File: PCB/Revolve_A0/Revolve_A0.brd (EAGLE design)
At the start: 123.9 x 100.1 mm, 442 parts, among them IC1 TMC2100-LA, IC10 74AHC1G126DCK, IC11 74AHC1G126DCK, IC12 TMC2100-LA, IC13 74AHC1G126DCK, IC14 74AHC1G126DCK, IC15 TMC2100-LA, IC16 74AHC1G126DCK, IC17 74AHC1G126DCK, IC18 74AHC1G126DCK, IC19 74AHC1G126DCK, IC2 TMC2100-LA, IC20 74AHC1G126DCK, IC21 74AHC1G126DCK, IC22 74AHC1G126DCK, IC24 TMC2100-LA, IC25 74AHC1G126DCK, IC26 74AHC1G126DCK, IC27 74AHC1G126DCK, IC28 74AHC1G126DCK, IC29 LAN8710A, IC3 74AHC1G126DCK, IC30 MTFC2GMDEA, IC31 CY7C65632, IC4 74AHC1G126DCK, IC5 TMC2100-LA, IC6 74AHC1G126DCK, IC7 74AHC1G126DCK, IC8 74AHC1G126DCK, IC9 74AHC1G126DCK, J1 USD_CONNECTOR, Q1 AON6758, Q2 AON6758, Q3 AON6758, Q8 AON6758, U1 SN74AHC595PW, U10 TPD4S012_DRY_6, U11 PCA9685PW, U18 CAT24C256, U19 CD4050BD, U2 SN74AHC595PW, U3 SN74AHC595PW, U4 SN74AHC595PW, U5 SN74AHC595PW, U6 RT8268, U8 SN74AHC595PW, X1 22-05-7038-03, X10 22-05-7038-03, X11 22-05-7038-03, X12 22-05-7048-04, X13 22-05-7038-03, X14 22-05-7048-04, X15 22-05-7048-04, X16 22-05-7048-04, X17 22-05-7048-04, X18 22-05-7048-04, X19 22-05-7038-03, X2 MSTBA4, X20 MSTBA4, X21 MSTBA2, X22 22-05-7038-03, X23 22-05-7038-03, X24 HDMI, X25 22-05-7048-04, X26 MSTBA2, X27 MINI-USB_SHIELD5P4-32005-400, X29 22-05-7038-03, X3 MSTBA2, X4 22-05-7028-02, X5 22-05-7028-02, X6 22-05-7028-02, X7 22-05-7038-03, X8 22-05-7038-03, X9 22-05-7028-02, Y1 24MHz, Y2 32.768 MHz, Y3 25 MHz, Y4 12 MHz

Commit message: Starting up work again
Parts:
- removed C14, C15, C24, C41, C42, C5, C84, C85, C86, C87, C88, C99: 0.1uF, rcl:C0402
- removed IC10, IC11, IC13, IC14, IC16, IC17, IC18, IC19, IC20, IC21, IC22, IC25, IC26, IC27, IC3, IC4, IC8, IC9: 74AHC1G126DCK, 74xx-little-de:SC70-5
- removed U1, U2, U3, U4, U5, U8: SN74AHC595PW, sn74hc595:SOP65P640X120-16N
- moved R151 61.5 mm to (102.5, 70.1)
- moved C155 55.6 mm to (102.8, 68.1)
- moved C154 13.7 mm to (119.0, 28.6), turned to 90 degrees
- moved C153 12.4 mm to (120.2, 28.6), turned to 90 degrees
- moved R88 4.49 mm to (105.7, 72.5)
- moved IC31 4.43 mm to (102.3, 70.5)
- moved R92 2.54 mm to (99.5, 85.0)
- moved R94 1.04 mm to (99.1, 88.8)
- moved C112 0.43 mm to (98.6, 77.5)
- moved C114 0.39 mm to (96.3, 77.5)
- moved C108 0.32 mm to (85.6, 84.7)
- moved C115 0.32 mm to (85.6, 85.8)
- moved U$7 0.32 mm to (92.8, 83.8)
- moved R93 0.12 mm to (99.1, 87.8)
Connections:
- removed net EN_EHA: IC19.2, IC22.2, IC27.2, U4.15
- removed net EN_XYZ: IC18.2, IC20.2, IC21.2, U1.15
- removed net N$103: IC17.1, U5.7
- removed net N$104: IC17.2, U5.6
- removed net N$105: IC16.1, U5.5
- removed net N$106: IC16.2, U5.4
- removed net N$142: IC26.1, U8.7
- removed net N$143: IC26.2, U8.6
- removed net N$144: IC25.2, U8.4
- removed net N$146: IC25.1, U8.5
- removed net N$34: IC3.2, U1.4
- removed net N$4: IC4.1, U1.7
- removed net N$40: IC3.1, U1.5
- removed net N$5: IC4.2, U1.6
- removed net N$59: IC11.1, U3.7
- removed net N$61: IC11.2, U3.6
- removed net N$62: IC10.1, U3.5
- removed net N$63: IC10.2, U3.4
- removed net N$66: IC9.1, U2.7
- removed net N$67: IC9.2, U2.6
- removed net N$68: IC8.1, U2.5
- removed net N$69: IC8.2, U2.4
- removed net N$85: IC14.1, U4.7
- removed net N$86: IC14.2, U4.6
- removed net N$87: IC13.1, U4.5
- removed net N$93: IC13.2, U4.4
- removed net SER6: U5.9
- removed net SER_2: U1.9, U2.14
- removed net SER_3: U2.9, U3.14
- removed net SER_4: U3.9, U4.14
- removed net SER_5: U4.9, U5.14
- removed net SER_6: U8.14
- removed net TRISTATE_STEPPERS: IC18.1, IC19.1, IC20.1, IC21.1, IC22.1, IC27.1, U5.15, U8.15
- net +3V3: no longer C14.1, C15.1, C24.1, C41.1, C42.1, C5.1, C84.1, C85.1, C86.1, C87.1, C88.1, C99.1, IC10.5, IC11.5, IC13.5, IC14.5, IC16.5, IC17.5, IC18.5, IC19.5, IC20.5, IC21.5, IC22.5, IC25.5, IC26.5, IC27.5, IC3.5, IC4.5, IC8.5, IC9.5, U1.10, U1.16, U2.10, U2.16, U3.10, U3.16, U4.10, U4.16, U5.10, U5.16, U8.10, U8.16
- net ENABLE_A: no longer IC27.4
- net ENABLE_E: no longer IC19.4
- net ENABLE_H: no longer IC22.4
- net ENABLE_X: no longer IC18.4
- net ENABLE_Y: no longer IC20.4
- net ENABLE_Z: no longer IC21.4
- net GND: no longer C14.2, C15.2, C24.2, C41.2, C42.2, C5.2, C84.2, C85.2, C86.2, C87.2, C88.2, C99.2, IC10.3, IC11.3, IC13.3, IC14.3, IC16.3, IC17.3, IC18.3, IC19.3, IC20.3, IC21.3, IC22.3, IC25.3, IC26.3, IC27.3, IC3.3, IC4.3, IC8.3, IC9.3, U1.13, U1.8, U2.13, U2.8, U3.13, U3.8, U4.13, U4.8, U5.13, U5.8, U8.13, U8.8
- net N$100: no longer U5.3
- net N$101: no longer U5.2
- net N$102: no longer U5.1
- net N$133: no longer IC25.4
- net N$138: no longer IC26.4
- net N$139: no longer U8.3
- net N$140: no longer U8.2
- net N$141: no longer U8.1
- net N$28: no longer IC10.4
- net N$42: no longer IC8.4
- net N$43: no longer U1.1
- net N$44: no longer U1.3
- net N$49: no longer IC9.4
- net N$53: no longer U2.3
- net N$54: no longer IC11.4
- net N$55: no longer U3.3
- net N$56: no longer U2.2
- net N$57: no longer U3.2
- net N$58: no longer U3.1
- net N$6: no longer U1.2
- net N$65: no longer U2.1
- net N$76: no longer IC13.4
- net N$81: no longer IC14.4
- net N$82: no longer U4.3
- net N$83: no longer U4.2
- net N$84: no longer U4.1
- net N$91: no longer IC16.4
- net N$99: no longer IC17.4
- net SERVO_0_EN: no longer U2.15
- net SERVO_1_EN: no longer U3.15
- net SPI1_CS1: no longer U1.12, U2.12, U3.12, U4.12, U5.12, U8.12
- net SPI1_MOSI: no longer U1.14
- net SPI1_SCLK: no longer U1.11, U2.11, U3.11, U4.11, U5.11, U8.11
- net X_CFG1: no longer IC4.4
- net X_CFG2: no longer IC3.4
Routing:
- net SYS_5V: track 20.0 -> 99.4 mm, vias 0 -> 4
- net SPI1_CS1: track 76.3 -> 8.89 mm, vias 5 -> 0
- net TRISTATE_STEPPERS: track 61.5 -> 0.00 mm, vias 6 -> 0
- net 12MHZ: track 0.00 -> 45.1 mm, vias 0 -> 2
- net EN_XYZ: track 39.5 -> 0.00 mm, vias 4 -> 0
- net N$186: track 0.00 -> 27.7 mm, vias 0 -> 2
- net EN_EHA: track 26.1 -> 0.00 mm, vias 3 -> 0
- net N$185: track 0.00 -> 23.2 mm, vias 0 -> 2
- net N$1: track 0.00 -> 20.4 mm, vias 0 -> 2
- net SPI1_SCLK: track 16.8 -> 0.00 mm, vias 2 -> 0
- net +3V3: track 237.3 -> 222.9 mm, vias 23 -> 20
- net SER_2: track 13.4 -> 0.00 mm, vias 2 -> 0
- net SER_5: track 12.9 -> 0.00 mm, vias 2 -> 0
- net SER_3: track 12.9 -> 0.00 mm, vias 2 -> 0
- net SER_4: track 12.1 -> 0.00 mm, vias 2 -> 0
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- added copper zone on layer 3, net HDMI_1V8

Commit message: Started porting to SIP-SM, changed to TMC2130
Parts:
- removed C13, C153: 0.1uF, rcl:C0402
- removed C154: 10uF, rcl:C0402
- removed IC28: 74AHC1G126DCK, 74xx-little-de:SC70-5
- removed J1: USD_CONNECTOR, BeagleBone_Blue:MICRO-SD-SOCKET-PP
- removed R142, R143, R144, R145, R146: 4.7K, rcl:R0402
- removed TP1, TP2, TP3, TP4: TPPAD1-13, testpad:P1-13
- removed U$10, U$8: IP4283CZ10-TBR, Revolve:UDFN
- removed U18: CAT24C256, custom:SOIC127P600X175-8N
- removed Y2: 32.768 MHz, Revolve:FX135A-327
- added C15, C24, C84, C85, C87, C99: 0.1uF, rcl:C0402
- added C41: 10uF, rcl:C0805
- added C42: 100uF, Panasonic-EEEFK_EEEFP:RHS1V10MCN1GS
- added C86: 4.7uF, rcl:C0402
- added C88: 22nF, rcl:C0402
- added EEPROM_WP, PMIC_NRESET, SYS_5V, SYS_RTC_1V8, SYS_VDD1_3V3, SYS_VDD2_3V3, SYS_VDD3_3V3, VDDS_DDR, VDDS_PLL, VDD_CODE, VDD_MPU: TPPAD1-13, testpad:P1-13
- added R153: 22R, rcl:R0402
- added SV2: (no value), con-lstb:MA05-1
- added U$11, U$12: DF10G7M1N, Revolve:DF10G7M1N
- added U1: OSD3358-512M-BSM, Octavo-Systems:OSD335X-BGA-256
- C144, C145: value 18pF -> 4.7uF
- C152: value 0.1uF -> 0.001uF
- R126: value 22R -> 2.2R
- R138: value 4.7K -> 0.1R; device rcl:R0402 -> rcl:R0805
- R139: value 1.5K -> 0.1R; device rcl:R0402 -> rcl:R0805
- R140: value 1.5K -> 10K
- R141: value 4.7K -> 10K
- R149: value 1M -> 0.1,5%
- U$2: value OSD3358-PARTS -> TRINAMIC_TMC2130_QFN36; device OSD3358-BAS-2:BGA400 -> TMC2130-Eval_v13:TRINAMIC_QFN36
- moved R141 307.0 mm to (-12.4, -250.9), turned to 0 degrees
- moved C145 297.9 mm to (-12.4, -241.4), turned to 0 degrees
- moved R126 297.4 mm to (-6.50, -210.3), turned to 0 degrees
- moved C144 295.5 mm to (-12.4, -236.6), turned to 0 degrees
- moved R140 291.9 mm to (-12.4, -246.1), turned to 0 degrees
- moved R138 283.1 mm to (-11.9, -225.2), turned to 0 degrees
- moved R139 276.9 mm to (-11.9, -231.2), turned to 0 degrees
- moved JP2 156.2 mm to (139.4, 89.3)
- moved R149 112.9 mm to (-12.4, -48.2), turned to 0 degrees
- moved C105 71.1 mm to (114.7, 10.1)
- moved LED10 71.1 mm to (121.8, 19.9)
- moved LED11 71.1 mm to (121.8, 18.8)
- moved LED12 71.1 mm to (121.8, 17.6)
- moved LED13 71.1 mm to (121.8, 8.22)
- moved LED9 71.1 mm to (121.8, 21.1)
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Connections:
- removed net GPIO1_16: U$2.R13
- removed net GPIO2_0: U$2.T13
- removed net GPIO3_21: U$2.V17
- removed net LCD_VCLK: R126.1, U$7.4
- removed net LDO_PGOOD: U$2.B20, U$2.B5
- removed net MMC0_CD: J1.CD1, R146.1, U$2.C15
- removed net MMC0_CLK: J1.CLK, R138.1, U$2.G17
- removed net MMC0_CMD: J1.CMD, R141.1, U$2.G18
- removed net MMC0_DAT0: J1.DAT0, R142.1, U$2.G16
- removed net MMC0_DAT1: J1.DAT1, R143.1, U$2.G15
- removed net MMC0_DAT2: J1.DAT2, R144.1, U$2.F18
- removed net MMC0_DAT3: J1.CD/DAT3, R145.1, U$2.F17
- removed net N$182: U$2.D13
- removed net N$211: U$2.R7
- removed net PMIC_INT: U$2.B19
- removed net PMIC_NWAKEUP: U$2.A19, U$2.C5
- removed net PMIC_PGOOD: IC28.2, U$2.A20, U$2.B15
- removed net PMIC_POWER_EN: U$2.C6, U$2.D19
- removed net SPI1_CS1: U$2.C18
- removed net SPI1_MISO: U$2.B13
- removed net SPI1_MOSI: U$2.D12
- removed net SPI1_SCLK: U$2.A13
- removed net VDD_1V8: L3.2, U$2.N16, U$2.R16
- removed net VDD_3V3A: U$2.E10, U$2.E11, U$2.E12, U$2.E13, U$2.F14, U$2.G14, U$2.H14, U$2.J14, U$2.K14, U$2.L14, U$2.N15, U$2.N5, U$2.P10, U$2.P11, U$2.P12, U$2.P13, U$2.P5, U$2.P6, U$2.P7, U$2.P8, U$2.R15
- removed net VDD_3V3AUX: R89.2, U$2.Y11
- removed net VDD_RTC: IC28.1, IC28.5, U$2.D7, U$2.E14, U$2.E6, U$2.F9, U$2.K13, U$2.N6, U$2.P14, U$2.P9
- new net CGND: R149.2
- new net DIR_B: U1.B15
- new net DIR_C: U1.R6
- new net IREF_X1: C145.1, R140.2, R141.1
- new net LCD_PCLK: R153.1, U$7.4, U1.F1
- new net N$103: U1.C10, U1.D10
- new net N$104: U1.C11, U1.D11
- new net N$105: SYS_VDD1_3V3.TP, U1.F6, U1.F7, U1.G6, U1.G7
- new net N$106: U$2.21
- new net N$120: SYS_VDD3_3V3.TP, U1.F8, U1.G8, U1.H7, U1.H8, U1.J7, U1.J8, U1.K8, U1.L8
- new net N$142: SYS_RTC_1V8.TP, U1.K11, U1.L11
- new net N$143: U1.L4, U1.M4
- new net N$144: U1.D4, U1.E4
- new net N$146: U1.F9, U1.G9, U1.H9, U1.J9, U1.K9, U1.L9
- new net N$161: U$2.20
- new net N$162: PMIC_NRESET.TP, U1.M13
- new net N$165: U1.T7
- new net N$166: C86.2, R126.1, U$2.25
- new net N$167: C87.1, R126.2, U$2.26
- new net N$168: C88.2, U$2.27
- new net N$170: C88.1, U$2.28
- new net N$171: C99.1, U$2.29
- new net N$188: U1.R12
- new net N$189: U1.P12
- new net N$190: U1.T13
- new net N$215: SV2.4, U1.A12
- new net N$34: U1.F4, VDDS_DDR.TP
- new net N$4: SV2.3, U1.C12
- new net N$40: U1.G4, VDD_CODE.TP
- new net N$5: SV2.2, U1.C13
- new net SPI0_CS0: U1.A14
- new net SPI0_CS1: U1.C14
- new net SPI0_CSX: U$2.2
- new net SPI0_MISO: U$2.5, U1.B13
- new net SPI0_MOSI: U$2.4, U1.B14
- new net SPI0_SCLK: U$2.3, U1.A13
- new net STEP_B: U1.B16
- new net STEP_C: U1.P6
- new net SYS_VDD2_3V3: R89.2, SYS_VDD2_3V3.TP, U1.F11, U1.G11
- new net SYS_VDD_1V8: L3.2, U1.F10, U1.G10, U1.H10, U1.H11, U1.J10, U1.J11, U1.K10, U1.L10
- new net VDDS_PLL: U1.G13, VDDS_PLL.TP
- new net VDD_MPU: U1.F13, VDD_MPU.TP
- new net VIN_BAT: U1.P8, U1.R8, U1.T8
- net +24V: now also C15.1, C24.1, C41.1, C42.+, C85.2, C99.2, U$2.16, U$2.30, U$2.31
- net +3V3: now also C84.1, U$2.8; no longer C13.1, C153.1, C154.1, J1.VCC, R138.2, R139.2, R140.2, R141.2, R142.2, R143.2, R144.2, R145.2, R146.2, U$2.U20, U$2.V20, U18.3, U18.8
- net +5V: now also U1.P10, U1.R10, U1.T10; no longer U$2.Y5, U$2.Y6
- net DIR_A: now also U1.A16
- net DIR_E: now also U1.C4; no longer U$2.U13
- net DIR_H: now also U1.C16; no longer U$2.V13
- net DIR_X: now also U$2.7, U1.A2; no longer U$2.V6
- net DIR_Y: now also U1.B1; no longer U$2.U10
- net DIR_Z: now also U1.B3; no longer U$2.T11
- net EMMC_RST: now also U1.R13; no longer U$2.R14
- net ENABLE: no longer U$2.D14
- net END_STOP_X_1: no longer U$2.A14
- net END_STOP_X_2: no longer U$2.T17
- net END_STOP_Y_1: no longer U$2.V14
- net END_STOP_Y_2: no longer U$2.C12
- net END_STOP_Z_1: no longer U$2.U17
- net END_STOP_Z_2: no longer U$2.B16
- net FAULT_E: no longer U$2.V12
- net FAULT_H: no longer U$2.T7
- net FAULT_X: no longer U$2.U6
- net FAULT_Y: no longer U$2.T6
- net FAULT_Z: no longer U$2.D15
- net GND: now also C144.2, C145.2, C15.2, C24.2, C41.2, C42.-, C84.2, C85.1, C86.1, C87.2, R138.1, R139.1, R149.1, SV2.1, U$11.3, U$12.3, U$2.11, U$2.12, U$2.24, U$2.35, U$2.36, U$2.GND_PAD, U1.D8, U1.D9, U1.E10, U1.E11, U1.E12, U1.E5, U1.E6, U1.E7, U1.E8, U1.E9, U1.F12, U1.F5, U1.G12, U1.G5, U1.H12, U1.H13, U1.H4, U1.H5, U1.J12, U1.J13, U1.J4, U1.J5, U1.K12, U1.K5, U1.L12, U1.L5, U1.M10, U1.M11, U1.M12, U1.M5, U1.M6, U1.M7, U1.M8, U1.M9, U1.N8, U1.N9; no longer C13.2, C153.2, C154.2, IC28.3, J1.GND, J1.GND1, J1.GND3, U$10.3, U$10.8, U$2.A1, U$2.A18, U$2.E19, U$2.E20, U$2.F19, U$2.F8, U$2.G11, U$2.G12, U$2.G19, U$2.G8, U$2.G9, U$2.H10, U$2.H12, U$2.H19, U$2.H6, U$2.H7, U$2.H8, U$2.H9, U$2.J10, U$2.J11, U$2.J19, U$2.J20, U$2.J6, U$2.J7, U$2.J8, U$2.J9, U$2.K10, U$2.K11, U$2.K19, U$2.K7, U$2.K9, U$2.L10, U$2.L11, U$2.L12, U$2.L13, U$2.L19, U$2.M10, U$2.M12, U$2.M14, U$2.M19, U$2.M6, U$2.M7, U$2.M8, U$2.M9, U$2.N10, U$2.N11, U$2.N14, U$2.N19, U$2.N20, U$2.N7, U$2.P19, U$2.P20, U$2.R19, U$2.R20, U$2.T19, U$2.T20, U$2.U19, U$2.V1, U$2.V18, U$2.V19, U$2.W10, U$2.W11, U$2.W12, U$2.W13, U$2.W14, U$2.W15, U$2.W16, U$2.W17, U$2.W18, U$2.W19, U$2.W2, U$2.W20, U$2.W3, U$2.W5, U$2.W6, U$2.W7, U$2.W8, U$2.W9, U$2.Y10, U$2.Y12, U$2.Y15, U$2.Y18, U$2.Y7, U$8.3, U$8.8, U18.1, U18.2, U18.4
- net GNDA_ADC: now also U1.A9; no longer U$2.A6, U$2.A9, U$2.E8
- net HDMI_INT: now also U1.T15; no longer U$2.U16
- net I2C0_SCL: no longer R140.1, U$2.C16, U$2.C20, U18.6
- net I2C0_SDA: no longer R139.1, U$2.C17, U$2.C19, U18.5
- net IREF_X_RAW: now also R141.2
- net LCD_D0: now also U1.G3; no longer U$2.R1
- net LCD_D1: now also U1.G2; no longer U$2.R2
- net LCD_D10: now also U1.K2; no longer U$2.U3
- net LCD_D11: now also U1.K1; no longer U$2.U4
- net LCD_D12: now also U1.L3; no longer U$2.V2
- net LCD_D13: now also U1.L2; no longer U$2.V3
- net LCD_D14: now also U1.L1; no longer U$2.V4
- net LCD_D15: now also U1.M3; no longer U$2.T5
- net LCD_D2: now also U1.G1; no longer U$2.R3
- net LCD_D3: now also U1.H3; no longer U$2.R4
- net LCD_D4: now also U1.H2; no longer U$2.T1
- net LCD_D5: now also U1.H1; no longer U$2.T2
- net LCD_D6: now also U1.J3; no longer U$2.T3
- net LCD_D7: now also U1.J2; no longer U$2.T4
- net LCD_D8: now also U1.J1; no longer U$2.U1
- net LCD_D9: now also U1.K3; no longer U$2.U2
- net LCD_DE: now also R153.2, U1.E1; no longer U$2.R6
- net LCD_HSYNC: now also U1.F2; no longer U$2.R5
- net LCD_VSYNC: now also U1.F3; no longer U$2.U5
- net MDIO_CLK: now also U1.D13; no longer U$2.M18
- net MDIO_DATA: now also U1.E13; no longer U$2.M17
- net MII1_COL: now also U1.F15; no longer U$2.H16
- net MII1_CRS_DV: now also U1.F14; no longer U$2.H17
- net MII1_RXCLK: now also U1.E16; no longer U$2.L18
- net MII1_RXD0: now also U1.E14; no longer U$2.M16
- net MII1_RXD1: now also U1.D16; no longer U$2.L15
- net MII1_RXD2: now also U1.D15; no longer U$2.L16
- net MII1_RXD3: now also U1.D14; no longer U$2.L17
- net MII1_RXDV: now also U1.F16; no longer U$2.J17
- net MII1_RXERR: now also U1.E15; no longer U$2.J15
- net MII1_TXCLK: now also U1.H16; no longer U$2.K18
- net MII1_TXD0: now also U1.H15; no longer U$2.K17
- net MII1_TXD1: now also U1.H14; no longer U$2.K16
- net MII1_TXD2: now also U1.G16; no longer U$2.K15
- net MII1_TXD3: now also U1.G15
- net MII1_TXEN: now also U1.G14; no longer U$2.J16, U$2.J18
- net MMC1_CLK: now also U1.P2; no longer U$2.U9
- net MMC1_CMD: now also U1.P1; no longer U$2.V9
- net MMC1_DAT0: now also U1.R3; no longer U$2.U7
- net MMC1_DAT1: now also U1.R2; no longer U$2.V7
- net MMC1_DAT2: now also U1.R1; no longer U$2.R8
- net MMC1_DAT3: now also U1.T3; no longer U$2.T8
- net MMC1_DAT4: now also U1.T2; no longer U$2.U8
- net MMC1_DAT5: now also U1.T1; no longer U$2.V8
- net MMC1_DAT6: now also U1.P4; no longer U$2.R9
- net MMC1_DAT7: now also U1.R4; no longer U$2.T9
- net N$1: now also U1.N10, U1.N11; no longer TP1.TP, U$2.E16
- net N$121: now also U1.N4, U1.N5; no longer TP2.TP, U$2.E15
- net N$172: now also R138.2, U$2.14; no longer C144.2, R149.1, U$2.H20, Y2.P$1
- net N$173: now also R139.2, U$2.33; no longer C145.2, R149.2, U$2.F20, Y2.P$2
- net N$174: now also EEPROM_WP.TP, U1.M2; no longer C144.1, C145.1, U$2.G20
- net N$175: no longer U$2.B10
- net N$176: now also U1.P16; no longer U$2.M20
- net N$177: now also U1.N15; no longer U$2.L20
- net N$178: now also U1.T16; no longer U$2.C13
- net N$179: now also U1.T11; no longer U$2.D20
- net N$184: now also U1.N16; no longer U$2.K20
- net N$185: now also C144.1, R140.1, U$2.23; no longer TP3.TP, U$2.E18
- net N$186: now also U1.T12; no longer TP4.TP, U$2.E17
- net N$210: now also SV2.5, U1.B12; no longer R126.2, U$2.V5
- net SERVO_0: no longer U$2.U14
- net SERVO_1: no longer U$2.T14
- net STEP_A: now also U1.A15
- net STEP_E: now also U1.C3; no longer U$2.U18
- net STEP_H: now also U1.C15; no longer U$2.R12
- net STEP_X: now also U$2.6, U1.A1; no longer U$2.U12
- net STEP_Y: now also U1.B2; no longer U$2.T12
- net STEP_Z: now also U1.A3; no longer U$2.T10
- net SYS_5V: now also SYS_5V.TP, U1.K6, U1.K7, U1.L6, U1.L7; no longer U$2.W4, U$2.Y4
- net SYS_RESETN: no longer IC28.4, U$2.A10
- net TERM_A: now also U1.C6; no longer U$2.A7
- net TERM_E: now also U1.A8; no longer U$2.B6
- net TERM_H: now also U1.B6; no longer U$2.B7
- net TERM_HBP: now also U1.B8; no longer U$2.C7
- net TX0+: now also U$12.5, U$12.6; no longer U$8.5
- net TX0-: now also U$12.4, U$12.7; no longer U$8.4
- net TX1+: now also U$11.2, U$11.9; no longer U$10.2
- net TX1-: now also U$11.1, U$11.10; no longer U$10.1
- net TX2+: now also U$11.5, U$11.6; no longer U$10.5
- net TX2-: now also U$11.4, U$11.7; no longer U$10.4
- net TXC+: now also U$12.2, U$12.9; no longer U$8.2
- net TXC-: now also U$12.1, U$12.10; no longer U$8.1
- net USB0_DM: now also U1.K16; no longer U$2.N18
- net USB0_DP: now also U1.K15; no longer U$2.N17
- net USB0_ID: now also U1.K14; no longer U$2.P16
- net USB1_DM: now also U1.L16; no longer U$2.R18
- net USB1_DP: now also U1.L15; no longer U$2.R17
- net USB1_OCN: now also U1.R15; no longer U$2.T16
- net USB_DC: now also U1.J16, U1.P9, U1.R9, U1.T9; no longer U$2.P15, U$2.Y8, U$2.Y9
- net USR0: now also U1.P13; no longer U$2.V15
- net USR1: now also U1.T14; no longer U$2.U15
- net USR2: now also U1.R14; no longer U$2.T15
- net USR3: now also U1.P14; no longer U$2.V16
- net VDD_ADC: now also U1.A7, U1.B7; no longer U$2.A4, U$2.A5, U$2.B9
- net XDMA_EVENT_INTR0: now also U1.A4; no longer U$2.A15
- net X_A1: now also U$2.34; no longer IC1.34
- net X_A2: now also U$2.32; no longer IC1.32
- net X_B1: now also U$2.13; no longer IC1.13
- net X_B2: now also U$2.15; no longer IC1.15
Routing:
- net MMC0_CLK: track 109.0 -> 0.00 mm, vias 4 -> 0
- net MMC0_DAT0: track 108.5 -> 0.00 mm, vias 4 -> 0
- net MMC0_DAT1: track 107.9 -> 0.00 mm, vias 4 -> 0
- net MMC0_DAT3: track 106.0 -> 0.00 mm, vias 4 -> 0
- net MMC0_CD: track 97.1 -> 0.00 mm, vias 2 -> 0
- net DIR_E: track 116.2 -> 26.0 mm, vias 7 -> 3
- net FAULT_E: track 109.7 -> 30.2 mm, vias 6 -> 3
- net USR3: track 78.4 -> 0.00 mm, vias 2 -> 0
- net MMC0_DAT2: track 77.5 -> 0.00 mm, vias 4 -> 0
- net USR0: track 77.2 -> 0.00 mm, vias 2 -> 0
- net USB1_DM: track 54.9 -> 0.00 mm, vias 1 -> 0
- net USB1_DP: track 53.8 -> 0.00 mm, vias 1 -> 0
- net MMC0_CMD: track 52.7 -> 0.00 mm, vias 3 -> 0
- net +3V3: track 222.9 -> 173.9 mm, vias 20 -> 18
- net LCD_VCLK: track 48.5 -> 0.00 mm, vias 4 -> 0
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
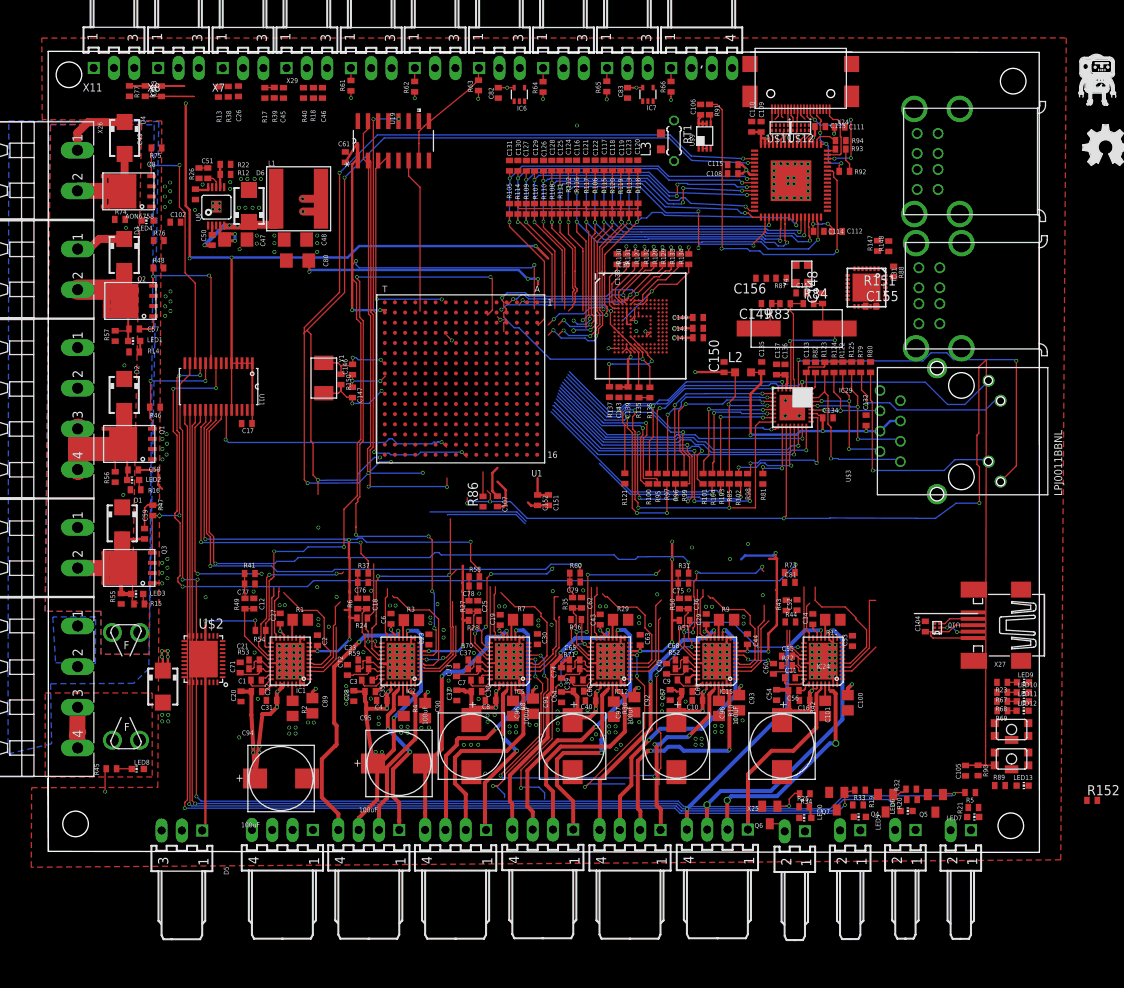
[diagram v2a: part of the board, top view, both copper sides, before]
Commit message: New Step down, moved some stuff around
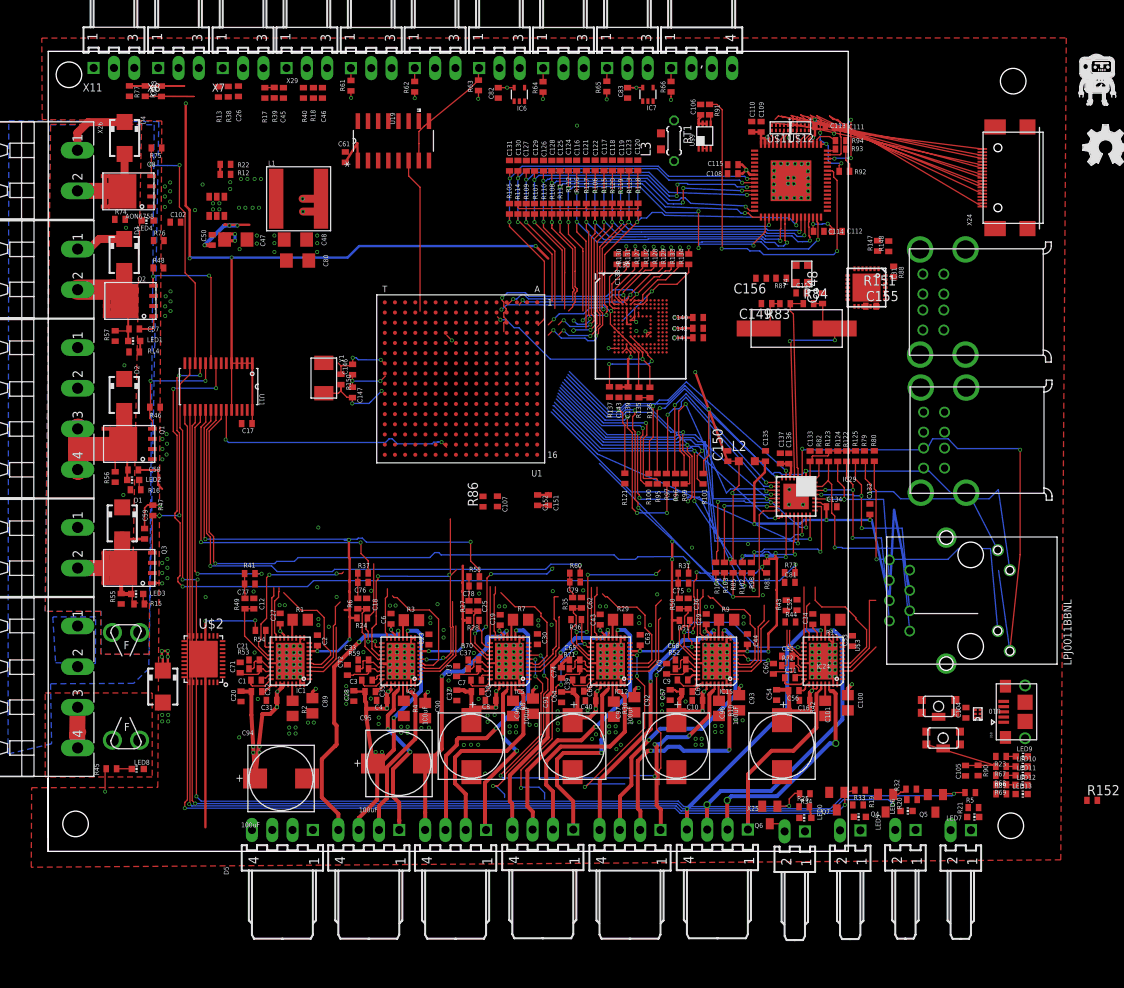
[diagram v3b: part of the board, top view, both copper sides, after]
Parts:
- removed C49: 10nF, rcl:C0402
- removed C51: 1nF, rcl:C0402
- removed D6: MBRA340T3, diode:SMA
- removed R26: 39K, rcl:R0402
- removed U6: RT8268, SparkFun:MSOP10
- removed X23: 22-05-7038-03, con-molex:7395-03
- removed X27: MINI-USB_SHIELD5P4-32005-400, con-cypressindustries:32005-400
- added U$10: TPS54202, Texas Instruments_By_element14_Batch_1:SOT23
- added U$8: USB-MICRO, Manga_screen_rev_B-3:USB-MICRO
- moved X24 26.3 mm to (118.4, 84.2), turned to 90 degrees
- moved U$3 21.2 mm to (115.3, 31.3)
- moved U$6 18.1 mm to (114.8, 51.4)
- moved U$5 17.6 mm to (114.7, 68.7)
- moved C104 11.9 mm to (114.7, 17.3)
- moved U10 11.9 mm to (116.2, 17.2)
- moved R125 11.1 mm to (100.9, 49.4)
- moved C132 11.1 mm to (102.7, 42.8)
- moved C133 11.1 mm to (95.2, 49.4)
- moved C134 11.1 mm to (97.9, 43.1)
- moved C135 11.1 mm to (89.7, 49.4)
- moved C136 11.1 mm to (92.6, 49.1)
- moved C137 11.1 mm to (91.5, 49.1)
- moved C150 11.1 mm to (85.0, 49.4)
- moved IC29 11.1 mm to (93.5, 44.4)
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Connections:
- net N$106 renamed FAULT_X1
- net N$161 renamed FAULT_X0
- removed net DALLAS_W1: X23.2
- removed net N$189: U1.P12
- removed net N$25: C50.2, D6.C, L1.P$2, U6.5
- removed net N$88: C51.1, U6.8
- removed net N$97: C51.2, R26.1
- net +24V: now also U$10.3; no longer U6.4
- net +3V3: no longer X23.1
- net D+: now also U$8.P$3; no longer X27.3
- net D-: now also U$8.P$2; no longer X27.2
- net ENABLE_X: now also U$2.22
- net GND: now also U$10.1, U$2.1, U$2.17, U$8.P$10, U$8.P$11, U$8.P$5, U$8.P$6, U$8.P$7, U$8.P$8, U$8.P$9; no longer C49.2, D6.A, R26.2, U6.6, U6.EP, X23.3, X27.5
- net HEATER_E: now also U1.P12; no longer U11.11
- net ID: now also U$8.P$4; no longer X27.4
- net N$23: now also U$10.4; no longer U6.7
- net N$60: now also C50.2, L1.P$2, U$10.2; no longer C49.1, U6.10
- net N$73: now also U$10.6; no longer U6.2
- net USB_DC: now also U$8.P$1; no longer X27.1
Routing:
- net SYS_RESETN: track 155.3 -> 12.6 mm, vias 4 -> 0
- net I2C0_SDA: track 107.3 -> 0.00 mm, vias 4 -> 0
- net I2C0_SCL: track 106.6 -> 0.00 mm, vias 4 -> 0
- net FAULT_X: track 87.9 -> 2.82 mm, vias 4 -> 0
- net DIR_Y: track 80.9 -> 0.00 mm, vias 6 -> 0
- net END_STOP_Y_2: track 57.4 -> 0.00 mm, vias 4 -> 0
- net END_STOP_X_1: track 52.6 -> 0.00 mm, vias 2 -> 0
- net END_STOP_Z_2: track 51.9 -> 0.00 mm, vias 2 -> 0
- net +5V: track 41.8 -> 10.5 mm, vias 11 -> 8
- net +3V3: track 173.9 -> 145.9 mm, vias 18 -> 16
- net END_STOP_Y_1: track 27.4 -> 0.00 mm, vias 2 -> 0
- net VDD_PHYA: track 42.1 -> 69.5 mm
- net TX2-: track 2.49 -> 27.6 mm
- net TX2+: track 2.92 -> 27.7 mm
- net TX1+: track 2.84 -> 27.6 mm
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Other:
- board size 123.9 x 100.1 mm -> 100 x 100 mm
